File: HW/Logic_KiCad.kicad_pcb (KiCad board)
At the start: 2 copper layers, 244 parts, among them J1 USB_B_Micro, Q1 Q_NPN_BCE, Q2 Q_NPN_BCE, Q3 Q_PMOS_DGS, Q4 Q_PMOS_DGS, Q5 Q_PMOS_DGS, Q6 Q_PMOS_DGS, Q7 Q_PMOS_DGS, SW1 SW_SPDT, SW2 button, SW3 button, SW4 button, SW5 button, SW6 button, SW7 button, SW8 button, U1 ESP32-PICO-D4, U2 CP2102N-A01-GQFN28, U3 SY8105, U4 Dual_battery, U5 TP4056

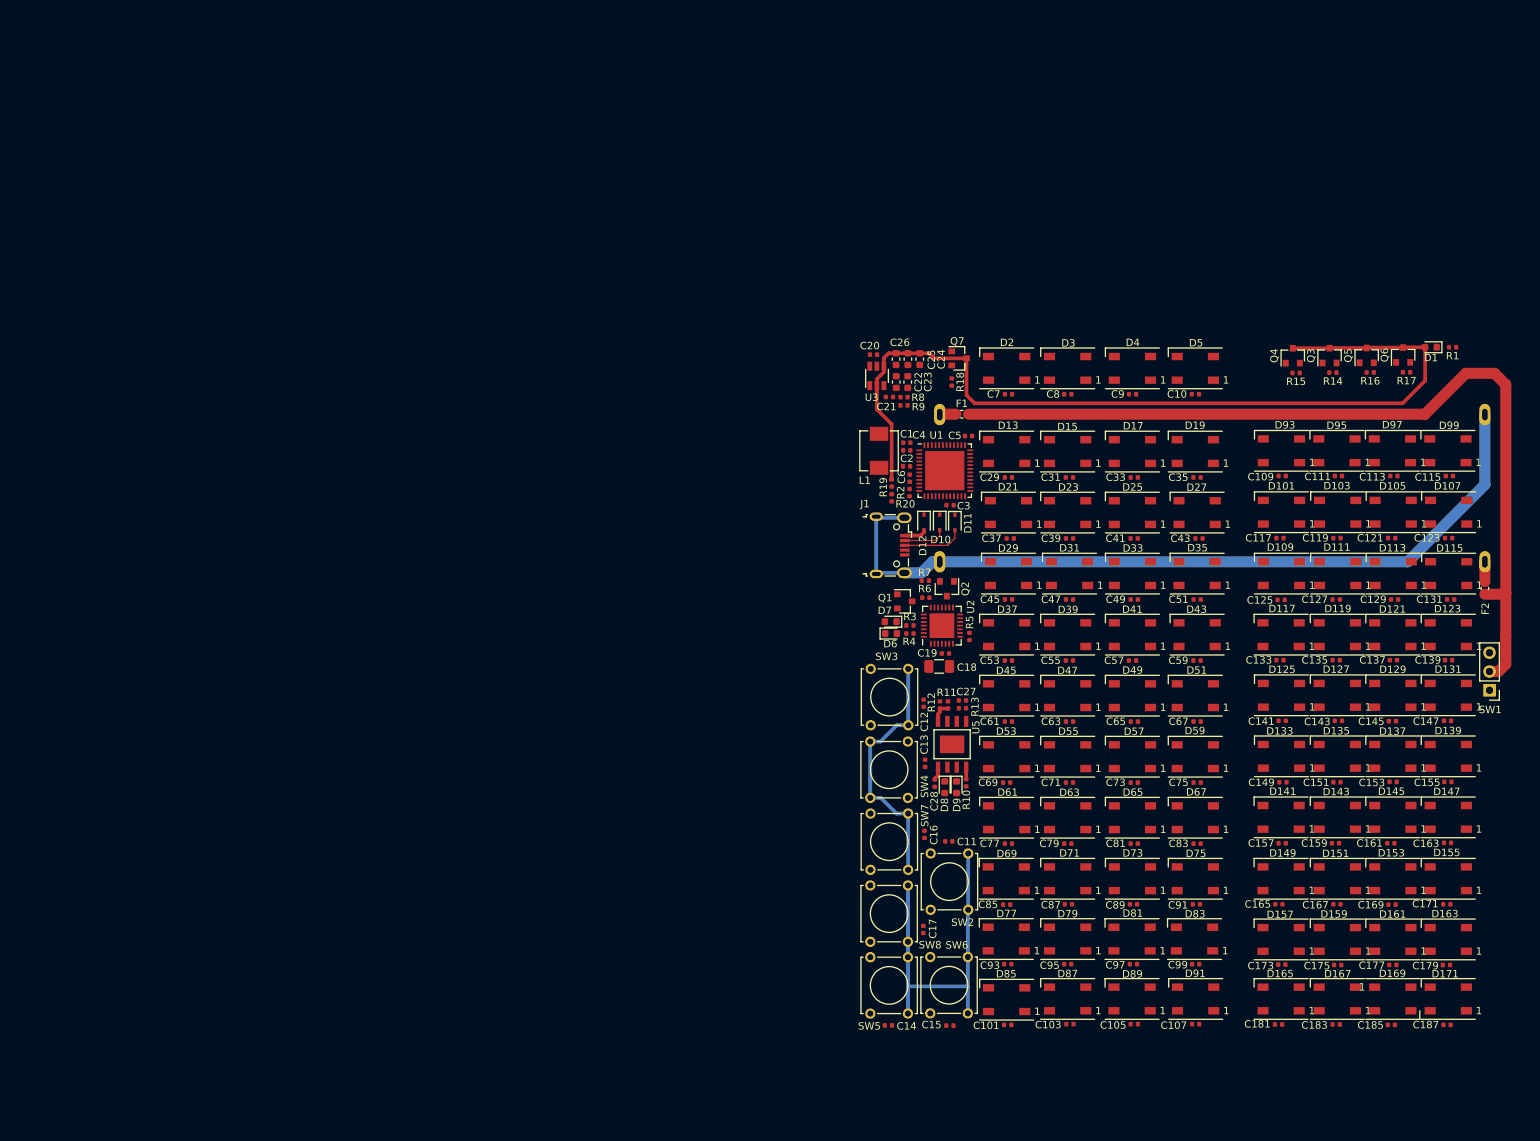
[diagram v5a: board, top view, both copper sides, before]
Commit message: make smaller test version, start routing
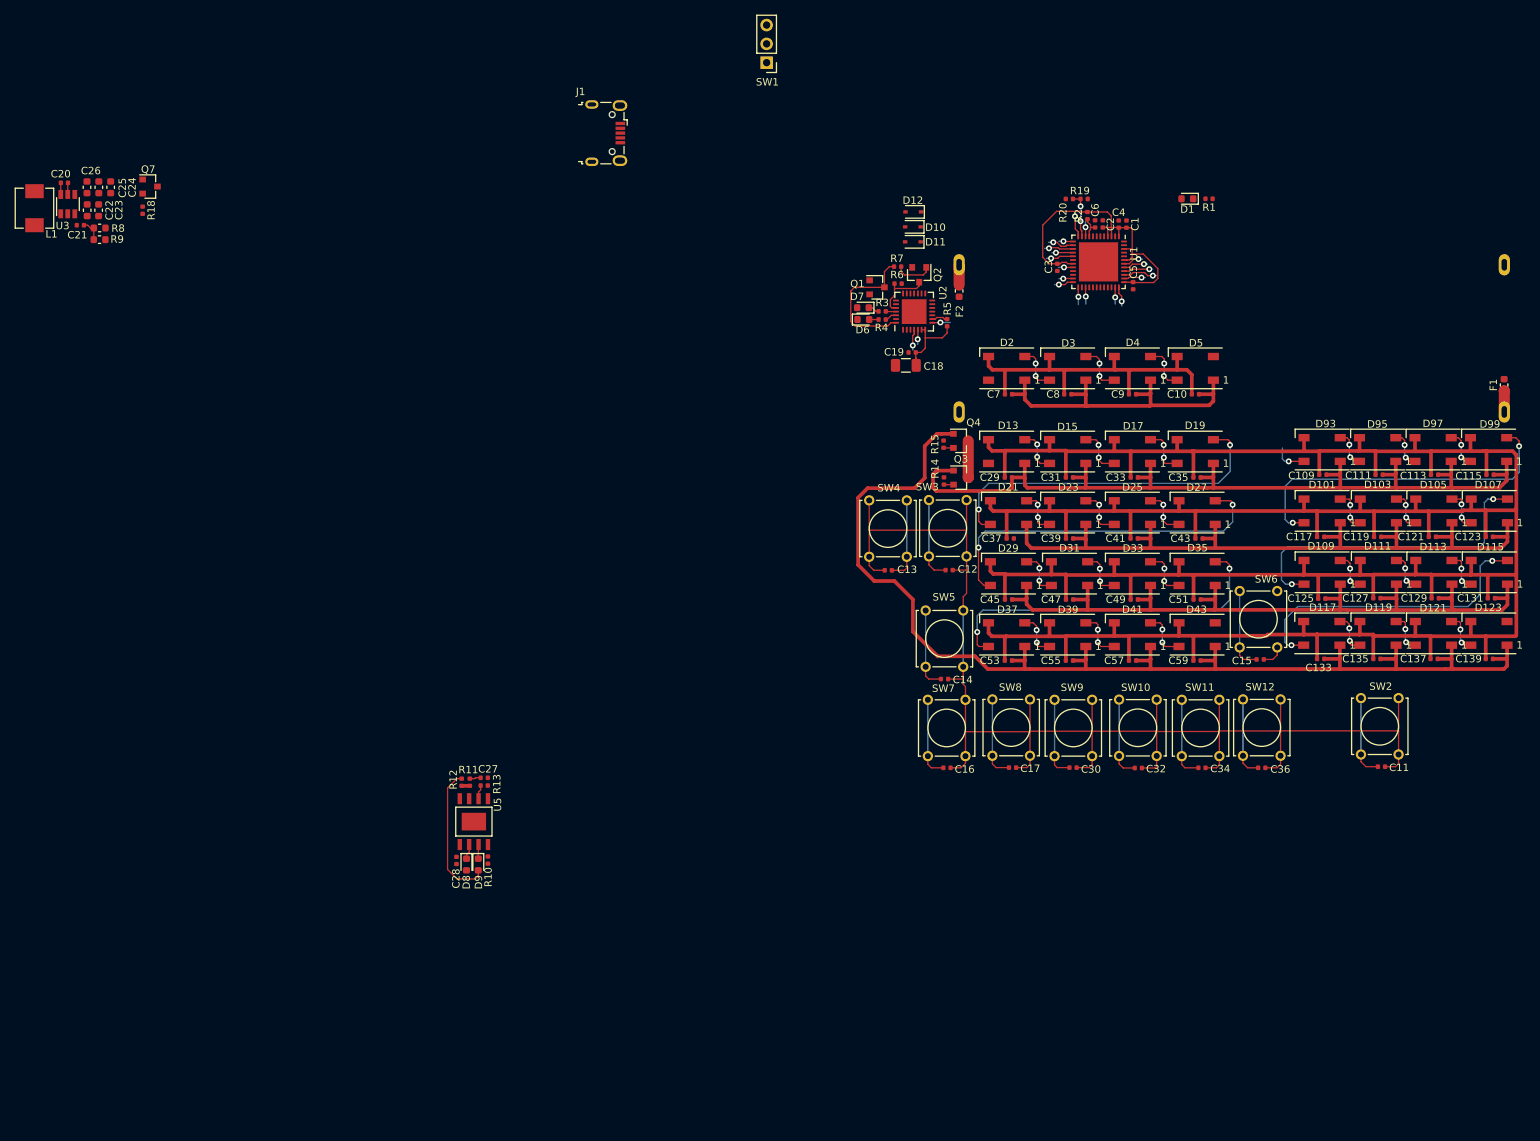
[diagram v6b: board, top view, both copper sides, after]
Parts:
- removed C101, C103, C105, C107, C141, C143, C145, C147, C149, C151, C153, C155, C157, C159, C161, C163, C165, C167, C169, C171, C173, C175, C177, C179, C181, C183, C185, C187, C61, C63, C65, C67, C69, C71, C73, C75, C77, C79, C81, C83, C85, C87, C89, C91, C93, C95, C97, C99: 100n, Capacitor_SMD:C_0402_1005Metric
- removed D125, D127, D129, D131, D133, D135, D137, D139, D141, D143, D145, D147, D149, D151, D153, D155, D157, D159, D161, D163, D165, D167, D169, D171, D45, D47, D49, D51, D53, D55, D57, D59, D61, D63, D65, D67, D69, D71, D73, D75, D77, D79, D81, D83, D85, D87, D89, D91: WS2812B, LED_SMD:LED_WS2812B_PLCC4_5.0x5.0mm_P3.2mm
- removed Q5, Q6: Q_PMOS_DGS, Package_TO_SOT_SMD:SOT-23
- removed R16, R17: 10k, Resistor_SMD:R_0402_1005Metric
- added C30: 10n, Capacitor_SMD:C_0402_1005Metric, F.Cu at (163.7, 94.2)
- added C32: 10n, Capacitor_SMD:C_0402_1005Metric, F.Cu at (172.6, 94.3)
- added C34: 10n, Capacitor_SMD:C_0402_1005Metric, F.Cu at (181.2, 94.2)
- added C36: 10n, Capacitor_SMD:C_0402_1005Metric, F.Cu at (189.2, 94.2)
- added SW10: button, Button_Switch_THT:SW_Tactile_Straight_KSL0Axx1LFTR, F.Cu at (169.9, 92.7)
- added SW11: button, Button_Switch_THT:SW_Tactile_Straight_KSL0Axx1LFTR, F.Cu at (178.4, 92.7)
- added SW12: button, Button_Switch_THT:SW_Tactile_Straight_KSL0Axx1LFTR, F.Cu at (186.7, 92.6)
- added SW9: button, Button_Switch_THT:SW_Tactile_Straight_KSL0Axx1LFTR, F.Cu at (161.2, 92.7)
- R8: value 200k -> 160k; footprint Resistor_SMD:R_0402_1005Metric -> Resistor_SMD:R_0603_1608Metric
- R9: value 44k2 -> 36k; footprint Resistor_SMD:R_0402_1005Metric -> Resistor_SMD:R_0603_1608Metric
- moved SW1 129.4 mm to (122.3, -1.07)
- moved L1 118.8 mm to (23.3, 18.6), turned to 90 degrees
- moved C26 111.8 mm to (30.4, 15.8)
- moved C20 111.8 mm to (27.4, 15.2)
- moved C21 111.8 mm to (29.5, 20.9)
- moved C23 111.8 mm to (32.0, 18.9)
- moved C24 111.8 mm to (33.6, 15.8)
- moved C25 111.8 mm to (32.0, 15.8)
- moved C22 111.8 mm to (30.4, 18.9)
- moved Q7 111.8 mm to (39.0, 15.7)
- moved R18 111.8 mm to (38.0, 18.9)
- moved U3 111.8 mm to (27.8, 18.1)
- moved R8 111.1 mm to (32.1, 21.3)
- moved R9 111.0 mm to (32.1, 22.9)
- moved F2 81.7 mm to (148.3, 29.8)
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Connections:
- net BTN_SIPKA_DOLU renamed BARVA_2
- net BTN_SIPKA_NAHORU renamed BARVA_1
- D123 pad 2: /hodnoceni_LED.sch/5.sch/DATA_IN -> (no net)
- D43 pad 2: /herni_LED.sch/5.sch/DATA_IN -> (no net)
- U1 pad 25: (no net) -> BARVA_5
- U1 pad 27: (no net) -> BARVA_6
- U1 pad 35: ZAPINANI_3_CAST_LED -> BARVA_4
- U1 pad 38: ZAPINANI_4_CAST_LED -> BARVA_3
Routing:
- net GND: track 190.4 -> 714.5 mm
- net V_BAT_1: track 0.00 -> 381.4 mm
- net V_BAT_2: track 0.00 -> 165.0 mm
- net V_BAT_PRIME: track 120.7 -> 0.00 mm
- net V_BAT: track 120.7 -> 4.98 mm
- net +3V3: track 0.02 -> 55.6 mm
- net /herni_LED.sch/3.sch/DATA_IN: track 0.00 -> 47.9 mm, vias 0 -> 2
- net /herni_LED.sch/4.ch/DATA_IN: track 0.00 -> 47.4 mm, vias 0 -> 2
- net /herni_LED.sch/2.sch/DATA_IN: track 0.00 -> 47.2 mm, vias 0 -> 2
- net /hodnoceni_LED.sch/2.sch/DATA_IN: track 0.00 -> 45.7 mm, vias 0 -> 2
- net /hodnoceni_LED.sch/3.sch/DATA_IN: track 0.00 -> 43.7 mm, vias 0 -> 2
- net /hodnoceni_LED.sch/4.ch/DATA_IN: track 0.00 -> 41.4 mm, vias 0 -> 2
- net Net-(Q1-Pad3): track 0.00 -> 19.1 mm
- net Net-(D9-Pad2): track 0.00 -> 19.0 mm
- net BTN_END: track 0.00 -> 15.3 mm, vias 0 -> 1
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
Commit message: continuation routing
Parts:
- moved C20 176.8 mm to (203.3, 33.1)
- moved C21 176.8 mm to (205.4, 38.9)
- moved C22 176.8 mm to (206.3, 36.8)
- moved C23 176.8 mm to (207.9, 36.8)
- moved C24 176.8 mm to (209.5, 33.7)
- moved C25 176.8 mm to (207.9, 33.7)
- moved L1 176.8 mm to (199.2, 36.5)
- moved R9 176.8 mm to (208.0, 40.8)
- moved U3 176.8 mm to (203.7, 36.0)
- moved C26 176.8 mm to (206.3, 33.7)
- moved Q7 176.8 mm to (214.8, 33.6)
- moved R18 176.8 mm to (213.8, 36.8)
- moved R8 176.8 mm to (208.0, 39.2)
- moved D8 156.3 mm to (213.0, 22.4), turned to 0 degrees
- moved C28 156.0 mm to (212.5, 23.8), turned to 0 degrees
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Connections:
- U1 pad 10: BARVA_2 -> BARVA_5
- U1 pad 15: BTN_END -> BTN_NEW_GAME
- U1 pad 16: BTN_NEW_GAME -> BTN_END
- U1 pad 20: ZAPINANI_2_CAST_LED -> ZAPINANI_1_CAST_LED
- U1 pad 24: ZAPINANI_1_CAST_LED -> ZAPINANI_2_CAST_LED
- U1 pad 25: BARVA_5 -> BARVA_2
- U1 pad 27: BARVA_6 -> BARVA_3
- U1 pad 38: BARVA_3 -> BARVA_6
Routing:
- net GND: track 714.5 -> 876.0 mm
- net BARVA_1: track 14.7 -> 139.5 mm
- net BTN_SIPKA_VLEVO: track 14.6 -> 139.2 mm, vias 1 -> 3
- net V_BAT_PRIME: track 0.00 -> 123.7 mm
- net BARVA_2: track 13.2 -> 115.3 mm
- net BTN_ENTER: track 14.7 -> 113.9 mm, vias 1 -> 5
- net BARVA_5: track 13.5 -> 105.9 mm, vias 1 -> 3
- net BARVA_3: track 13.9 -> 106.3 mm
- net BARVA_4: track 13.3 -> 94.6 mm
- net BTN_SIPKA_VPRAVO: track 13.1 -> 92.7 mm, vias 1 -> 5
- net VBUS: track 3.54 -> 77.1 mm, vias 1 -> 4
- net BARVA_6: track 13.2 -> 79.9 mm
- net V_BAT: track 4.98 -> 68.3 mm
- net BTN_NEW_GAME: track 14.1 -> 70.6 mm
- net BTN_END: track 15.3 -> 67.4 mm
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
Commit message: finishing routing, make fab
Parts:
- moved C15 66.6 mm to (140.1, 124.8)
- moved SW11 66.6 mm to (129.5, 137.8)
- moved SW2 66.6 mm to (153.7, 137.6)
- moved SW6 66.6 mm to (137.3, 123.1)
- moved C109 66.6 mm to (148.6, 99.8)
- moved C11 66.6 mm to (156.5, 139.3)
- moved C111 66.6 mm to (156.2, 99.8)
- moved C113 66.6 mm to (163.7, 99.8)
- moved C115 66.6 mm to (171.2, 99.8)
- moved C119 66.6 mm to (156.0, 108.2)
- moved C12 66.6 mm to (98.0, 112.7)
- moved C121 66.6 mm to (163.4, 108.2)
- moved C123 66.6 mm to (171.1, 108.2)
- moved C125 66.6 mm to (148.4, 116.5)
- moved C127 66.6 mm to (155.9, 116.5)
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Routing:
- net GND: track 876.0 -> 1030.6 mm, vias 0 -> 31
- net V_BAT_SPINANE: track 13.6 -> 101.2 mm
- net V_BAT: track 68.3 -> 152.4 mm, vias 0 -> 2
- net +3V3: track 46.4 -> 107.5 mm, vias 0 -> 8
- net VBUS: track 77.1 -> 120.6 mm, vias 4 -> 8
- net V_BAT_1: track 384.6 -> 402.9 mm, vias 0 -> 2
- net V_BAT_2: track 166.0 -> 153.1 mm, vias 0 -> 2
- net Net-(C20-Pad1): track 0.00 -> 8.98 mm
- net Net-(D1-Pad1): track 0.00 -> 1.78 mm
- net BARVA_2: track 115.3 -> 114.4 mm
- net IO0: track 33.4 -> 32.6 mm
- net BARVA_5: track 105.9 -> 105.2 mm
- net BTN_SIPKA_VPRAVO: track 92.7 -> 92.1 mm
- net BARVA_4: track 94.6 -> 94.1 mm
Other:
- board outline added: 92.5 x 82.5 mm
- rule trace_min: 0.09 -> 0.127
- rule via_min_drill: 0.3 -> 0.2
- rule via_min_size: 0.4 -> 0.45
